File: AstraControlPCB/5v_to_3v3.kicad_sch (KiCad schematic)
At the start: 18 parts, among them U3 ST1S12GR

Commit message: update
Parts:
- removed C12, C15: 47u, LiveAstra:C_0805_2012Metric_Pad1.18x1.45mm_HandSolder, symbol LiveAstra:C_47u_X5R_0805
- added C12, C15: DNP, LiveAstra:C_0805_2012Metric_Pad1.18x1.45mm_HandSolder, symbol LiveAstra:C_DNP_0805
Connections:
- net 3V3: now also C15.2
- net GND: now also C12.1, C15.1
- net SW_OUT_UNFILTERED: now also C12.2
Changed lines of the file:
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@@
-	)
-	(symbol
-		(lib_id "LiveAstra:C_47u_X5R_0805")
-		(at 187.96 129.54 90)
-		(unit 1)
-		(exclude_from_sim no)
-		(in_bom no)
-		(on_board yes)
-		(dnp yes)
-		(fields_autoplaced yes)
-		(property "Reference" "C12"
-			(at 191.77 126.9999 90)
-			(effects
-				(font
-					(size 1.27 1.27)
-				)
-				(justify right)
-			)
-		)
-		(property "Value" "47u"
-			(at 191.77 129.54 90)
-			(effects
-				(font
-					(size 1.27 1.27)
-					(bold yes)
-				)
-				(justify right)
-			)
-		)
-		(property "Footprint" "LiveAstra:C_0805_2012Metric_Pad1.18x1.45mm_HandSolder"
-			(at 196.85 129.54 0)
-			(effects
-				(font
-					(size 1.27 1.27)
-				)
-				(hide yes)
-			)
-		)
-		(property "Datasheet" "https://lcsc.com/product-detail/Multilayer-Ceramic-Capacitors-MLCC-SMD-SMT_SAMSUNG_CL21A476MQYNNNE_47uF-476-20-6-3V_C16780.html"
-			(at 200.66 129.54 0)
-			(effects
-				(font
-					(size 1.27 1.27)
-				)
-				(hide yes)
-			)
-		)
-		(property "Description" "Multilayer Ceramic Capacitor"
-			(at 193.04 129.54 0)
-			(effects
-				(font
-					(size 1.27 1.27)
-				)
-				(hide yes)
-			)
-		)
-		(property "LCSC Part" "C16780"
-			(at 204.47 129.54 0)
-			(effects
-				(font
-					(size 1.27 1.27)
-				)
-				(hide yes)
-			)
-		)
-		(property "Extra Values" "6.3V X5R 20% 0805"
-			(at 191.77 132.0799 90)
-			(effects
-				(font
-					(size 0.762 0.762)
-					(bold yes)
-				)
-				(justify right)
-			)
-		)
-		(pin "1"
-		)
-		(pin "2"
-		)
-		(instances
-			(project "AstraControl"
-				(path "/9a751838-dce8-4d69-8a02-736625ac74e7/0db21d8e-3390-4d67-877f-0e5d98e37848/2f1fbce1-3ac7-4103-a887-0795f5671ada"
-					(reference "C12")
-					(unit 1)
-				)
-			)
-		)
 	)
 	(symbol
@@
 	)
 	(symbol
-		(lib_id "LiveAstra:C_47u_X5R_0805")
+		(lib_id "LiveAstra:C_DNP_0805")
 		(at 251.46 129.54 90)
 		(unit 1)
@@
 			)
 		)
-		(property "Value" "47u"
+		(property "Value" "DNP"
 			(at 255.27 129.54 90)
 			(effects
@@
 			)
 		)
-		(property "Datasheet" "https://lcsc.com/product-detail/Multilayer-Ceramic-Capacitors-MLCC-SMD-SMT_SAMSUNG_CL21A476MQYNNNE_47uF-476-20-6-3V_C16780.html"
+		(property "Datasheet" ""
 			(at 264.16 129.54 0)
 			(effects
@@
 			)
 		)
-		(property "LCSC Part" "C16780"
+		(property "LCSC Part" ""
 			(at 267.97 129.54 0)
 			(effects
@@
 			)
 		)
-		(property "Extra Values" "6.3V X5R 20% 0805"
+		(property "Extra Values" "0805"
 			(at 255.27 132.0799 90)
 			(effects
@@
 					(unit 1)
 				)
+			)
+		)
+	)
+	(symbol
+		(lib_id "LiveAstra:C_DNP_0805")
+		(at 187.96 129.54 90)
+		(unit 1)
+		(exclude_from_sim no)
+		(in_bom no)
+		(on_board yes)
+		(dnp yes)
+		(fields_autoplaced yes)
+		(property "Reference" "C12"
+			(at 191.77 126.9999 90)
+			(effects
+				(font
+					(size 1.27 1.27)
+				)
+				(justify right)
+			)
+		)
+		(property "Value" "DNP"
+			(at 191.77 129.54 90)
+			(effects
+				(font
+					(size 1.27 1.27)
+					(bold yes)
+				)
+				(justify right)
+			)
+		)
+		(property "Footprint" "LiveAstra:C_0805_2012Metric_Pad1.18x1.45mm_HandSolder"
+			(at 196.85 129.54 0)
+			(effects
+				(font
+					(size 1.27 1.27)
+				)
+				(hide yes)
+			)
+		)
+		(property "Datasheet" ""
+			(at 200.66 129.54 0)
+			(effects
+				(font
+					(size 1.27 1.27)
+				)
+				(hide yes)
+			)
+		)
+		(property "Description" "Multilayer Ceramic Capacitor"
+			(at 193.04 129.54 0)
+			(effects
+				(font
+					(size 1.27 1.27)
+				)
+				(hide yes)
+			)
+		)
+		(property "LCSC Part" ""
+			(at 204.47 129.54 0)
+			(effects
+				(font
+					(size 1.27 1.27)
+				)
+				(hide yes)
+			)
+		)
+		(property "Extra Values" "0805"
+			(at 191.77 132.0799 90)
+			(effects
+				(font
+					(size 0.762 0.762)
+					(bold yes)
+				)
+				(justify right)
+			)
+		)
+		(pin "1"
+		)
+		(pin "2"
+		)
+		(instances
+			(project "AstraControl"
+				(path "/9a751838-dce8-4d69-8a02-736625ac74e7/0db21d8e-3390-4d67-877f-0e5d98e37848/2f1fbce1-3ac7-4103-a887-0795f5671ada"
+					(reference "C12")
+					(unit 1)
+				)

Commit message: Another redesign
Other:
- moved on the sheet: C9, R9
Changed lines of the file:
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@@
+	)
+	(junction
+		(at 187.96 101.6)
+		(diameter 0)
+		(color 0 0 0 0)
+	)
+	(junction
+		(at 121.92 101.6)
+		(diameter 0)
+		(color 0 0 0 0)
+	)
+	(junction
+		(at 48.26 101.6)
+		(diameter 0)
+		(color 0 0 0 0)
+	)
+	(junction
+		(at 177.8 101.6)
+		(diameter 0)
+		(color 0 0 0 0)
 	)
 	(junction
@@
 	)
 	(junction
-		(at 187.96 101.6)
+		(at 269.24 101.6)
 		(diameter 0)
 		(color 0 0 0 0)
 	)
 	(junction
-		(at 121.92 101.6)
-		(diameter 0)
-		(color 0 0 0 0)
-	)
-	(junction
-		(at 48.26 101.6)
-		(diameter 0)
-		(color 0 0 0 0)
-	)
-	(junction
-		(at 177.8 101.6)
-		(diameter 0)
-		(color 0 0 0 0)
-	)
-	(junction
-		(at 269.24 101.6)
+		(at 40.64 101.6)
 		(diameter 0)
 		(color 0 0 0 0)
@@
 	)
 	(junction
-		(at 35.56 101.6)
-		(diameter 0)
-		(color 0 0 0 0)
-	)
-	(junction
 		(at 232.41 101.6)
 		(diameter 0)
@@
 	(wire
 		(pts
-			(xy 35.56 101.6) (xy 35.56 116.84)
-		)
-		(stroke
-			(width 0)
-			(type default)
-		)
-	)
-	(wire
-		(pts
-			(xy 27.94 101.6) (xy 35.56 101.6)
+			(xy 27.94 101.6) (xy 27.94 132.08)
+		)
+		(stroke
+			(width 0)
+			(type default)
+		)
+	)
+	(wire
+		(pts
+			(xy 25.4 101.6) (xy 27.94 101.6)
 		)
 		(stroke
@@
 	(wire
 		(pts
+			(xy 27.94 101.6) (xy 40.64 101.6)
+		)
+		(stroke
+			(width 0)
+			(type default)
+		)
+	)
+	(wire
+		(pts
 			(xy 204.47 104.14) (xy 204.47 101.6)
 		)
@@
 	(wire
 		(pts
-			(xy 27.94 101.6) (xy 27.94 119.38)
-		)
-		(stroke
-			(width 0)
-			(type default)
-		)
-	)
-	(wire
-		(pts
-			(xy 25.4 101.6) (xy 27.94 101.6)
-		)
-		(stroke
-			(width 0)
-			(type default)
-		)
-	)
-	(wire
-		(pts
 			(xy 251.46 124.46) (xy 251.46 101.6)
 		)
@@
 	(wire
 		(pts
-			(xy 27.94 130.81) (xy 27.94 129.54)
+			(xy 40.64 113.03) (xy 40.64 111.76)
 		)
 		(stroke
@@
 	(wire
 		(pts
-			(xy 53.34 116.84) (xy 58.42 116.84)
+			(xy 45.72 132.08) (xy 55.88 132.08)
 		)
 		(stroke
@@
 	(wire
 		(pts
-			(xy 35.56 116.84) (xy 43.18 116.84)
+			(xy 40.64 101.6) (xy 48.26 101.6)
+		)
+		(stroke
+			(width 0)
+			(type default)
+		)
+	)
+	(wire
+		(pts
+			(xy 27.94 132.08) (xy 35.56 132.08)
+		)
+		(stroke
+			(width 0)
+			(type default)
+		)
+	)
+	(wire
+		(pts
+			(xy 55.88 116.84) (xy 58.42 116.84)
+		)
+		(stroke
+			(width 0)
+			(type default)
+		)
+	)
+	(wire
+		(pts
+			(xy 55.88 132.08) (xy 55.88 116.84)
 		)
 		(stroke
@@
 		(pts
 			(xy 101.6 101.6) (xy 83.82 101.6)
-		)
-		(stroke
-			(width 0)
-			(type default)
-		)
-	)
-	(wire
-		(pts
-			(xy 35.56 101.6) (xy 48.26 101.6)
 		)
 		(stroke
@@
 	)
 	(label "EN"
-		(at 53.34 116.84 0)
+		(at 55.88 116.84 0)
 		(fields_autoplaced yes)
 		(effects
@@
 	(symbol
 		(lib_id "LiveAstra:R_1MOhm_0805_125mW")
-		(at 48.26 116.84 180)
+		(at 40.64 132.08 180)
 		(unit 1)
 		(exclude_from_sim no)
@@
 		(fields_autoplaced yes)
 		(property "Reference" "R9"
-			(at 48.26 107.95 0)
+			(at 40.64 123.19 0)
 			(effects
 				(font
@@
 		)
 		(property "Value" "1M"
-			(at 48.26 110.49 0)
+			(at 40.64 125.73 0)
 			(effects
 				(font
@@
 		)
 		(property "Footprint" "LiveAstra:R_0805_2012Metric_Pad1.20x1.40mm_HandSolder"
-			(at 48.26 107.95 0)
+			(at 40.64 123.19 0)
 			(effects
 				(font
@@
 		)
 		(property "Datasheet" "https://lcsc.com/product-detail/Chip-Resistor-Surface-Mount-UniOhm_1MR-1004-1_C17514.html"
-			(at 48.26 104.14 0)
+			(at 40.64 119.38 0)
 			(effects
 				(font
@@
 		)
 		(property "Description" "Chip Resistor - Surface Mount ROHS"
-			(at 48.26 111.76 0)
+			(at 40.64 127 0)
 			(effects
 				(font
@@
 		)
 		(property "LCSC Part" "C17514"
-			(at 48.26 100.33 0)
+			(at 40.64 115.57 0)
 			(effects
 				(font
@@
 		)
 		(property "Extra Values" "150V 1% 0805 125mW"
-			(at 48.26 113.03 0)
+			(at 40.64 128.27 0)
 			(effects
 				(font
@@
 	(symbol
 		(lib_id "power:GND")
-		(at 27.94 130.81 0)
+		(at 40.64 113.03 0)
 		(unit 1)
 		(exclude_from_sim no)
@@
 		(fields_autoplaced yes)
 		(property "Reference" "#PWR021"
-			(at 27.94 137.16 0)
+			(at 40.64 119.38 0)
 			(effects
 				(font
@@
 		)
 		(property "Value" "GND"
-			(at 27.94 135.89 0)
+			(at 40.64 118.11 0)
 			(effects
 				(font
@@
 		)
 		(property "Footprint" ""
-			(at 27.94 130.81 0)
+			(at 40.64 113.03 0)
 			(effects
 				(font
@@
 		)
 		(property "Datasheet" ""
-			(at 27.94 130.81 0)
+			(at 40.64 113.03 0)
 			(effects
 				(font
@@
 		)
 		(property "Description" "Power symbol creates a global label with name \"GND\" , ground"
-			(at 27.94 130.81 0)
+			(at 40.64 113.03 0)
 			(effects
 				(font
@@
 	(symbol
 		(lib_id "LiveAstra:C_4u7_X5R_0603")
-		(at 27.94 124.46 90)
+		(at 40.64 106.68 90)
 		(unit 1)
 		(exclude_from_sim no)
@@
 		(fields_autoplaced yes)
 		(property "Reference" "C9"
-			(at 31.75 121.9199 90)
+			(at 44.45 104.1399 90)
 			(effects
 				(font
@@
 		)
 		(property "Value" "4u7"
-			(at 31.75 124.46 90)
+			(at 44.45 106.68 90)
 			(effects
 				(font
@@
 		)
 		(property "Footprint" "LiveAstra:C_0603_1608Metric"
-			(at 36.83 124.46 0)
+			(at 49.53 106.68 0)
 			(effects
 				(font
@@
 		)
 		(property "Datasheet" "https://lcsc.com/product-detail/Multilayer-Ceramic-Capacitors-MLCC-SMD-SMT_SAMSUNG_CL10A475KO8NNNC_4-7uF-475-10-16V_C19666.html"
-			(at 40.64 124.46 0)
+			(at 53.34 106.68 0)
 			(effects
 				(font
@@
 		)
 		(property "Description" "Surface mount ceramic multilayer capacitor"
-			(at 33.02 124.46 0)
+			(at 45.72 106.68 0)
 			(effects
 				(font
@@
 		)
 		(property "LCSC Part" "C19666"
-			(at 43.18 124.46 0)
+			(at 55.88 106.68 0)
 			(effects
 				(font
@@
 		)
 		(property "Extra Values" "16V X5R 10% 0603"
-			(at 31.75 126.9999 90)
-			(effects
-				(font
+			(at 44.45 109.2199 90)
+			(effects
+				(font

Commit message: Fixed fab layer
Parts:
- C12, C15: footprint LiveAstra:C_0805_2012Metric_Pad1.18x1.45mm_HandSolder -> LiveAstra:C_DNP_0805_2012Metric_Pad1.18x1.45mm_HandSolder
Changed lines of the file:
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@@
 			)
 		)
-		(property "Footprint" "LiveAstra:C_0805_2012Metric_Pad1.18x1.45mm_HandSolder"
+		(property "Footprint" "LiveAstra:C_DNP_0805_2012Metric_Pad1.18x1.45mm_HandSolder"
 			(at 260.35 129.54 0)
 			(effects
@@
 			)
 		)
-		(property "Footprint" "LiveAstra:C_0805_2012Metric_Pad1.18x1.45mm_HandSolder"
+		(property "Footprint" "LiveAstra:C_DNP_0805_2012Metric_Pad1.18x1.45mm_HandSolder"
 			(at 196.85 129.54 0)
 			(effects

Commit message: Updates
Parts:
- L1: Extra Values 4A 20% 41mΩ -> 4A 20% 41mOhm
- L2: Extra Values 1A 20% 1.3A 30mΩ -> 1A 20% 1.3A 30mOhm
- renumbered R9 to R10, R10 to R11, R11 to R12
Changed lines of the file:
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@@
 			)
 		)
-		(property "Extra Values" "1A 20% 1.3A 30mΩ"
+		(property "Extra Values" "1A 20% 1.3A 30mOhm"
 			(at 219.71 99.06 0)
 			(effects
@@
 		(dnp no)
 		(fields_autoplaced yes)
-		(property "Reference" "R9"
+		(property "Reference" "R10"
 			(at 40.64 123.19 0)
 			(effects
@@
 			(project ""
 				(path "/9a751838-dce8-4d69-8a02-736625ac74e7/0db21d8e-3390-4d67-877f-0e5d98e37848/2f1fbce1-3ac7-4103-a887-0795f5671ada"
-					(reference "R9")
+					(reference "R10")
 					(unit 1)
 				)
@@
 			)
 		)
-		(property "Datasheet" ""
+		(property "Datasheet" "https://www.lcsc.com/product-detail/Thimble-Copper-Rod-Test-Ring_ronghe-RH-5000_C5277086.html"
 			(at 254 93.98 90)
 			(effects
@@
 		(dnp no)
 		(fields_autoplaced yes)
-		(property "Reference" "R11"
+		(property "Reference" "R12"
 			(at 124.46 121.9199 90)
 			(effects
@@
 			(project "AstraControl"
 				(path "/9a751838-dce8-4d69-8a02-736625ac74e7/0db21d8e-3390-4d67-877f-0e5d98e37848/2f1fbce1-3ac7-4103-a887-0795f5671ada"
-					(reference "R11")
+					(reference "R12")
 					(unit 1)
 				)
@@
 		(dnp no)
 		(fields_autoplaced yes)
-		(property "Reference" "R10"
+		(property "Reference" "R11"
 			(at 124.46 106.6799 90)
 			(effects
@@
 			(project "AstraControl"
 				(path "/9a751838-dce8-4d69-8a02-736625ac74e7/0db21d8e-3390-4d67-877f-0e5d98e37848/2f1fbce1-3ac7-4103-a887-0795f5671ada"
-					(reference "R10")
+					(reference "R11")
 					(unit 1)
 				)
@@
 			)
 		)
-		(property "Datasheet" ""
+		(property "Datasheet" "https://www.lcsc.com/product-detail/Thimble-Copper-Rod-Test-Ring_ronghe-RH-5000_C5277086.html"
 			(at 177.8 93.98 90)
 			(effects
@@
 			)
 		)
-		(property "Datasheet" ""
+		(property "Datasheet" "https://www.lcsc.com/product-detail/Thimble-Copper-Rod-Test-Ring_ronghe-RH-5000_C5277086.html"
 			(at 48.26 93.98 90)
 			(effects
@@
 			)
 		)
-		(property "Extra Values" "4A 20% 41mΩ"
+		(property "Extra Values" "4A 20% 41mOhm"
 			(at 106.68 99.06 0)
 			(effects

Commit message: Added MFN MPR to each components for eurocircuits
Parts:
- C10, C11, C9: MFN (none) -> Samsung Electro-Mechanics; MPN (none) -> CL10A475KO8NNNC
- C13: MFN (none) -> Samsung Electro-Mechanics; MPN (none) -> CL10A226MQ8NRNC
- C14: MFN (none) -> Samsung Electro-Mechanics; MPN (none) -> CL21A476MQYNNNE
- L1: MFN (none) -> KOHERelec; MPN (none) -> MDA4020-2R2M
- L2: MFN (none) -> Sunlord; MPN (none) -> SWPA4030S220MT
- R10: MFN (none) -> UNI-ROYAL(Uniroyal Elec); MPN (none) -> 0805W8F1004T5E
- R11: MFN (none) -> UNI-ROYAL(Uniroyal Elec); MPN (none) -> 0402WGF4532TCE
- R12: MFN (none) -> UNI-ROYAL(Uniroyal Elec); MPN (none) -> 0402WGF1002TCE
- TP7, TP8, TP9: MFN (none) -> ronghe; MPN (none) -> RH-5000
- U3: MFN (none) -> STMicroelectronics; MPN (none) -> ST1S12GR

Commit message: Update schematic titles, templates
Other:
- title: AstraControl - Root -> AstraControl - 5V to 3.3V
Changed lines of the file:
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@@
 	(paper "A4")
 	(title_block
-		(title "AstraControl - Root")
+		(title "AstraControl - 5V to 3.3V")
 		(date "2024-08-26")
 		(rev "A")

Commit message: Updated Pi filter
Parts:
- removed C13: 22u, LiveAstra:C_0603_1608Metric, symbol LiveAstra:C_22uF_X5R_0603
- removed C14: 47u, LiveAstra:C_0805_2012Metric_Pad1.18x1.45mm_HandSolder, symbol LiveAstra:C_47u_X5R_0805
- removed L2: 22uH, LiveAstra:L_Sunlord_SWPA4030S, symbol LiveAstra:L_22uH_1A_ SWPA4030S220MT
- added C13, C14: 4u7, LiveAstra:C_0603_1608Metric, symbol LiveAstra:C_4u7_X5R_0603
- added L2: 2u2H, LiveAstra:L_MDA4020_4.1x4.5mm, symbol LiveAstra:L_2u2H_4A_MDA4020-2R2M
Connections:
- net 3V3: now also C14.2, L2.1
- net GND: now also C13.1, C14.1
- net SW_OUT_UNFILTERED: now also C13.2, L2.2
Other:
- note added: "PI Filter: Cutoff frequency: -3dB at 40KHz Mostly for educational purposes."
- note removed: "PI Filter: Cutoff frequency: 8.76kHz Mostly for educational purposes."

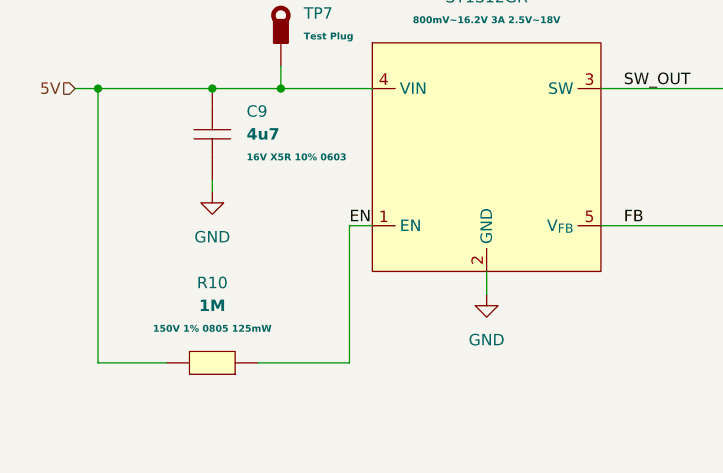
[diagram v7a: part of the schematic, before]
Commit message: Prepare for review, silkscreen updates, minor tweaks
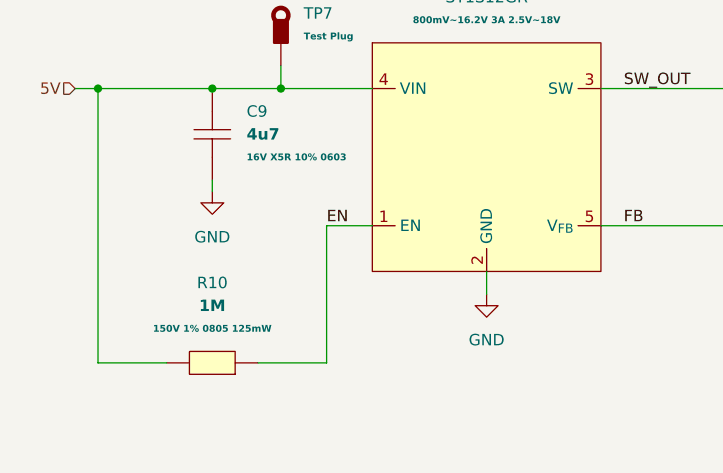
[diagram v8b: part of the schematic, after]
